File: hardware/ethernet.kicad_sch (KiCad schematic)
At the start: 92 parts, among them J5 USB_C_Receptacle, Q1 BSS138, Q2 BSS138, U11 TXS0202YZPR, U14 KSZ9031RNXCA, U4 GateMate-CCGM1A1, X1 ECS-2520MV-250-xx

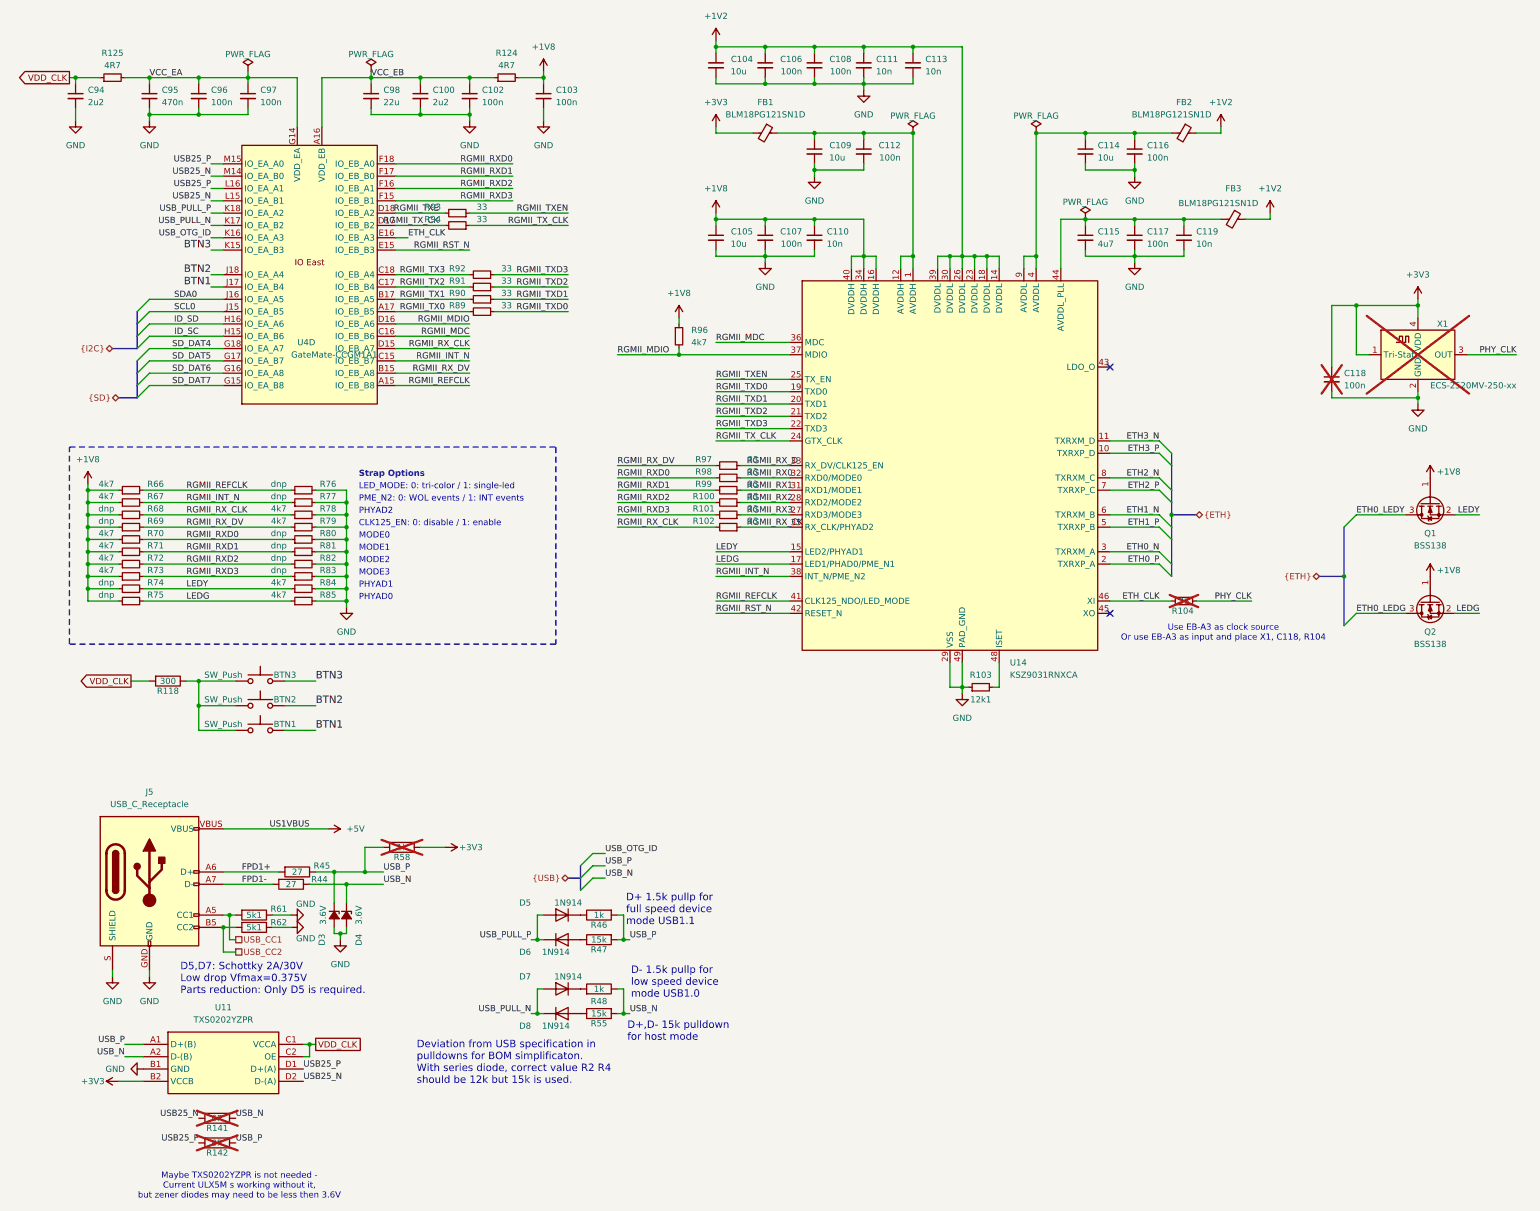
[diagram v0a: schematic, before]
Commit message: Updating sch - moving power select resistors to bottom
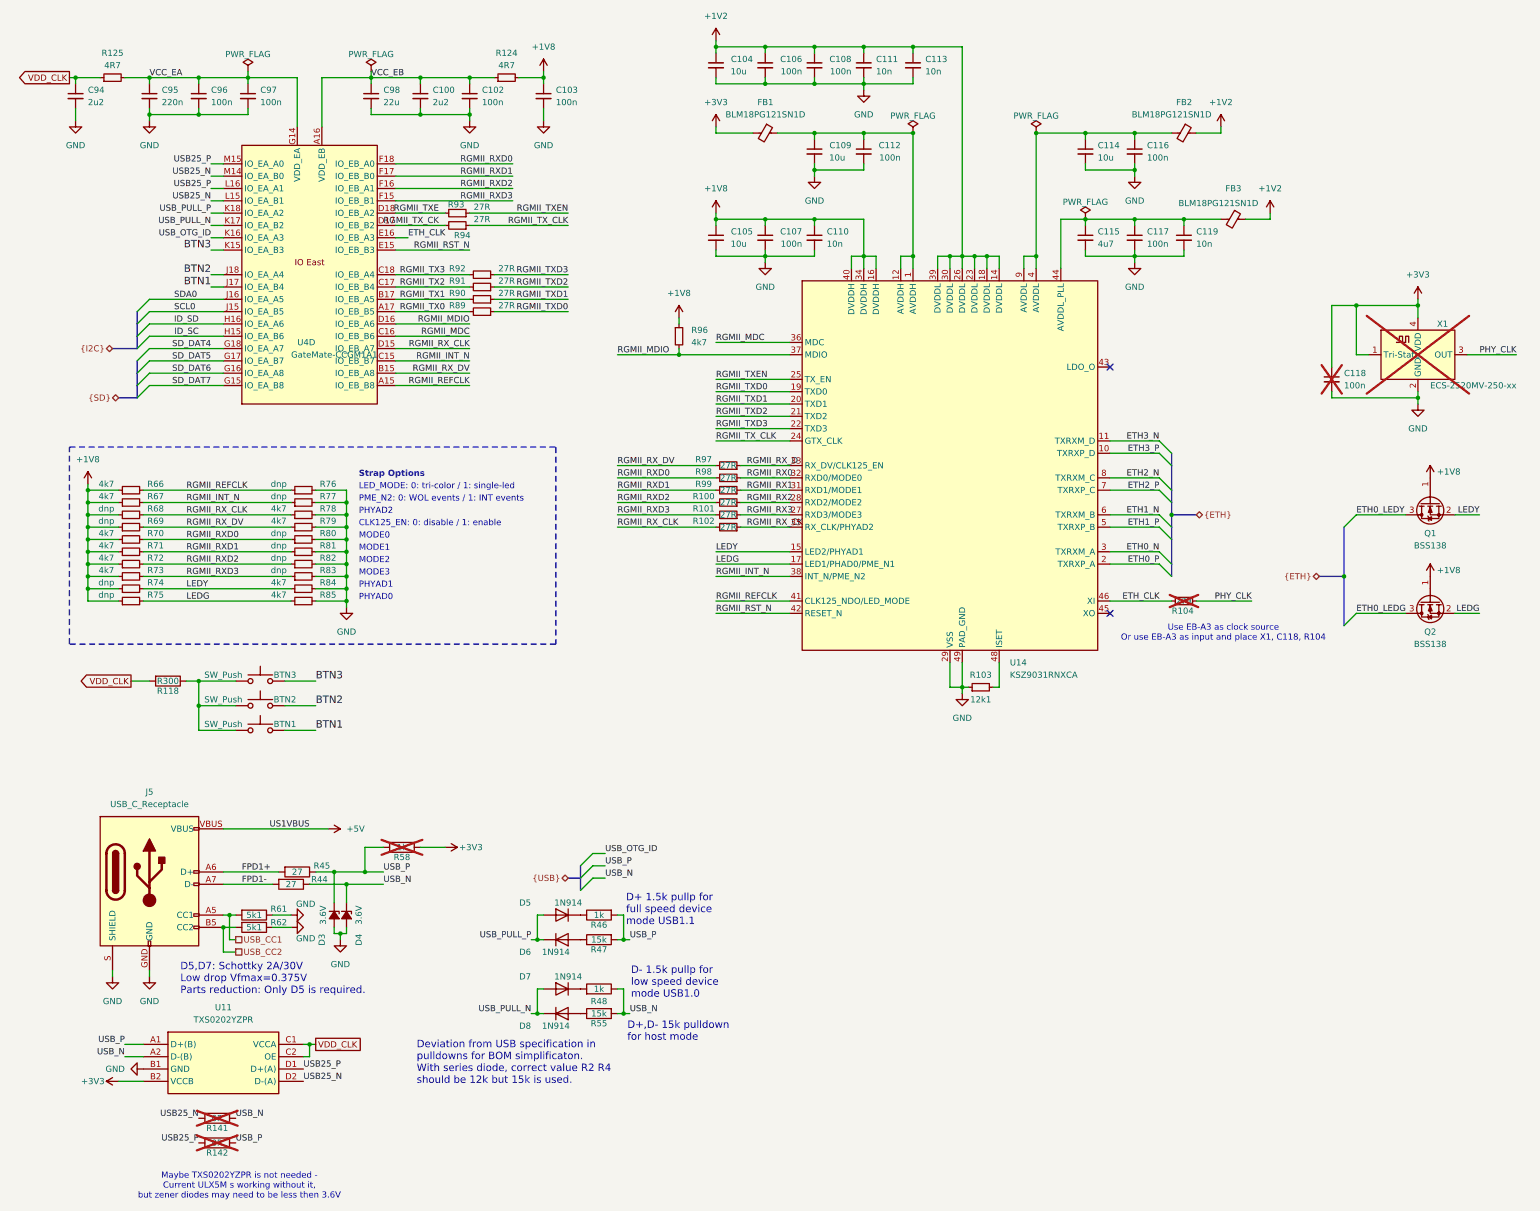
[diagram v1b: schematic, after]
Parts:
- C95: value 470n -> 220n
- R100, R101, R102, R104, R89, R90, R91, R92, R93, R94, R97, R98, R99: value 33 -> 27R
- R118: value 300 -> R300
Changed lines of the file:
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@@
 		(fields_autoplaced yes)
 		(property "Reference" "C95"
-			(at 43.18 29.2163 0)
+			(at 43.18 29.2162 0)
 			(effects
 				(font
@@
 			)
 		)
-		(property "Value" "470n"
-			(at 43.18 31.7563 0)
+		(property "Value" "220n"
+			(at 43.18 31.7562 0)
 			(effects
 				(font
@@
 		(dnp no)
 		(property "Reference" "R93"
-			(at 99.06 53.34 90)
+			(at 103.886 52.832 90)
 			(effects
 				(font
@@
 			)
 		)
-		(property "Value" "33"
+		(property "Value" "27R"
 			(at 109.22 53.34 90)
 			(effects
@@
 			)
 		)
-		(property "Value" "33"
-			(at 165.1 110.49 90)
+		(property "Value" "27R"
+			(at 160.02 111.76 90)
 			(effects
 				(font
@@
 			)
 		)
-		(property "Value" "33"
-			(at 165.1 107.95 90)
+		(property "Value" "27R"
+			(at 160.02 109.22 90)
 			(effects
 				(font
@@
 			)
 		)
-		(property "Value" "300"
+		(property "Value" "R300"
 			(at 44.45 151.13 90)
 			(effects
@@
 			)
 		)
-		(property "Value" "33"
+		(property "Value" "27R"
 			(at 114.3 73.66 90)
 			(effects
@@
 			)
 		)
-		(property "Value" "33"
-			(at 165.1 115.57 90)
+		(property "Value" "27R"
+			(at 160.02 116.84 90)
 			(effects
 				(font
@@
 			)
 		)
-		(property "Value" "33"
+		(property "Value" "27R"
 			(at 114.3 71.12 90)
 			(effects
@@
 			)
 		)
-		(property "Value" "33"
-			(at 165.1 113.03 90)
+		(property "Value" "27R"
+			(at 160.02 114.3 90)
 			(effects
 				(font
@@
 			)
 		)
-		(property "Value" "33"
+		(property "Value" "27R"
 			(at 114.3 68.58 90)
 			(effects
@@
 			)
 		)
-		(property "Value" "33"
+		(property "Value" "27R"
 			(at 114.3 66.04 90)
 			(effects
@@
 			)
 		)
-		(property "Value" "33"
+		(property "Value" "27R"
 			(at 254 134.62 90)
 			(effects
@@
 			)
 		)
-		(property "Value" "33"
-			(at 165.1 118.11 90)
+		(property "Value" "27R"
+			(at 160.02 119.38 90)
 			(effects
 				(font
@@
 			)
 		)
-		(property "Value" "33"
-			(at 165.1 105.41 90)
+		(property "Value" "27R"
+			(at 160.02 106.68 90)
 			(effects
 				(font
@@
 		(dnp no)
 		(property "Reference" "R94"
-			(at 99.06 55.88 90)
+			(at 105.156 59.182 90)
 			(effects
 				(font
@@
 			)
 		)
-		(property "Value" "33"
+		(property "Value" "27R"
 			(at 109.22 55.88 90)
 			(effects

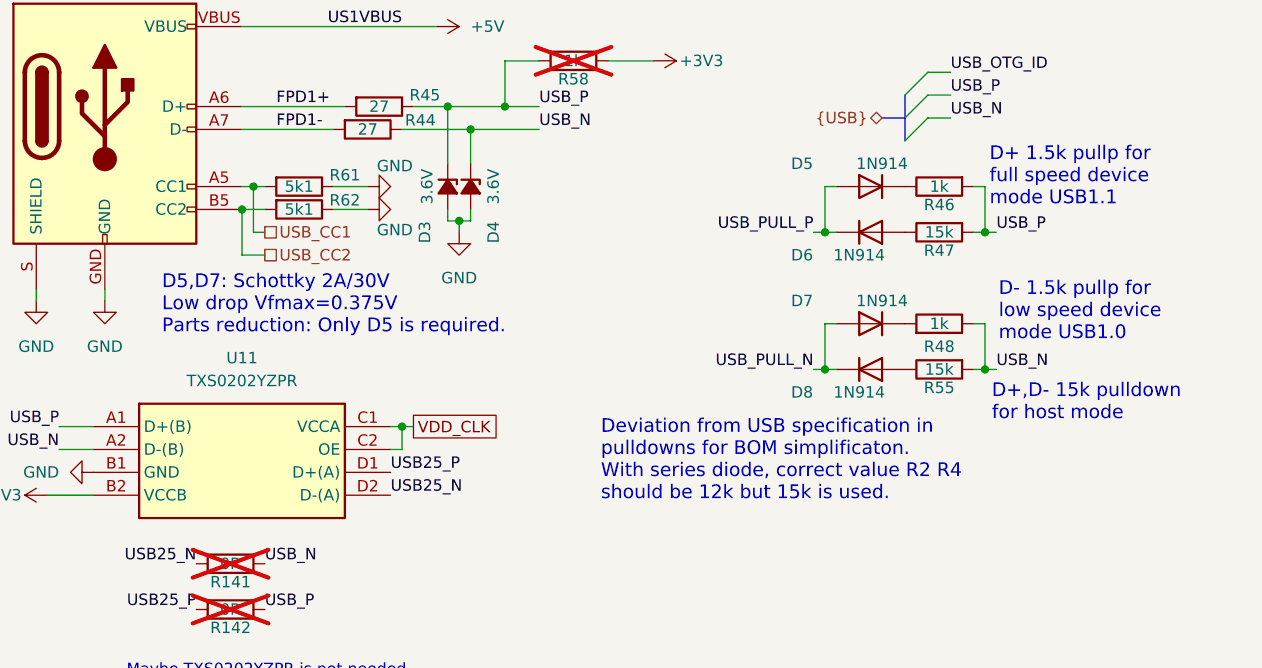
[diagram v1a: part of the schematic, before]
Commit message: USB PULL resistors can now be 12K
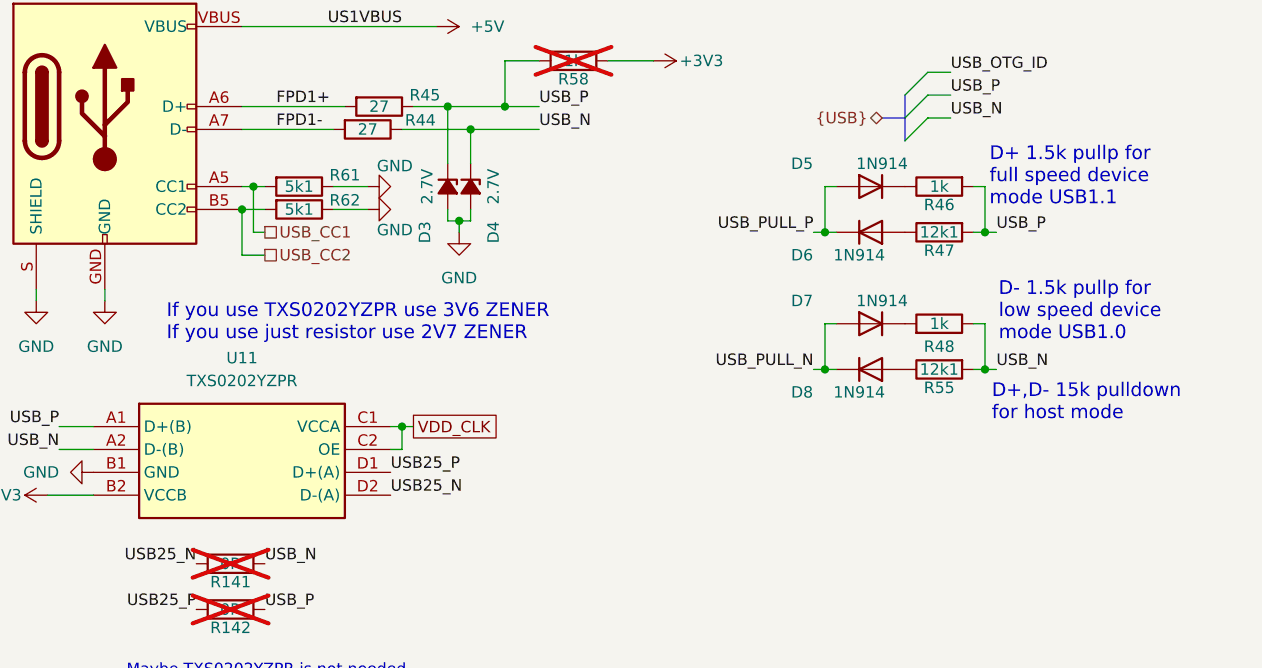
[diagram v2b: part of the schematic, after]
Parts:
- D3, D4: value 3.6V -> 2.7V
- R47, R55: value 15k -> 12k1
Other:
- note added: "If you use TXS0202YZPR use 3V6 ZENER If you use just resistor use 2V7 ZENER"
- note removed: "D5,D7: Schottky 2A/30V Low drop Vfmax=0.375V Parts reduction: Only D5 is required."
- note removed: "Deviation from USB specification in pulldowns for BOM simplificaton. With series diode, correct value R2 R4 should be 12k but 15k is used."
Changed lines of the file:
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@@
 		)
 	)
-	(text "Deviation from USB specification in\npulldowns for BOM simplificaton.\nWith series diode, correct value R2 R4 \nshould be 12k but 15k is used."
-		(exclude_from_sim no)
-		(at 95.758 234.442 0)
-		(effects
-			(font
-				(size 1.524 1.524)
-			)
-			(justify left bottom)
-		)
-	)
 	(text "MODE0"
 		(exclude_from_sim no)
@@
 		)
 	)
+	(text "If you use TXS0202YZPR use 3V6 ZENER\nIf you use just resistor use 2V7 ZENER"
+		(exclude_from_sim no)
+		(at 47.498 216.662 0)
+		(effects
+			(font
+				(size 1.524 1.524)
+			)
+			(justify left bottom)
+		)
+	)
 	(text "MODE2"
 		(exclude_from_sim no)
@@
 		)
 	)
-	(text "D5,D7: Schottky 2A/30V \nLow drop Vfmax=0.375V\nParts reduction: Only D5 is required."
-		(exclude_from_sim no)
-		(at 46.99 215.9 0)
-		(effects
-			(font
-				(size 1.524 1.524)
-			)
-			(justify left bottom)
-		)
-	)
 	(text "D- 1.5k pullp for \nlow speed device\nmode USB1.0"
 		(exclude_from_sim no)
@@
 			)
 		)
-		(property "Value" "3.6V"
+		(property "Value" "2.7V"
 			(at 76.454 199.39 0)
 			(effects
@@
 			)
 		)
-		(property "Value" "15k"
+		(property "Value" "12k1"
 			(at 133.35 219.71 90)
 			(effects
@@
 			)
 		)
-		(property "Value" "3.6V"
+		(property "Value" "2.7V"
 			(at 83.82 199.39 0)
 			(effects
@@
 			)
 		)
-		(property "Value" "15k"
+		(property "Value" "12k1"
 			(at 133.35 204.47 90)
 			(effects

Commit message: Fix #19
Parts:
- added R144, R145, R146: 1K, Resistor_SMD:R_0402_1005Metric, symbol Device:R
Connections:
- net BTN1: now also R144.2
- net BTN2: now also R145.2
- net BTN3: now also R146.2
- net GND: now also R118.2
- net VDD_CLK: now also R144.1, R145.1, R146.1; no longer R118.2
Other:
- moved on the sheet: BTN1, BTN2, BTN3, R118

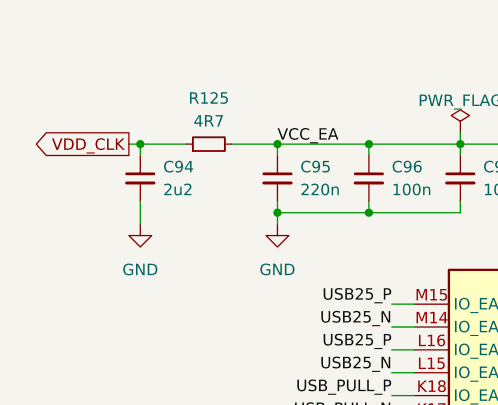
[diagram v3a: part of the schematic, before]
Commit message: Moving VCC_EA to 3.3V - USB and GPIO #27
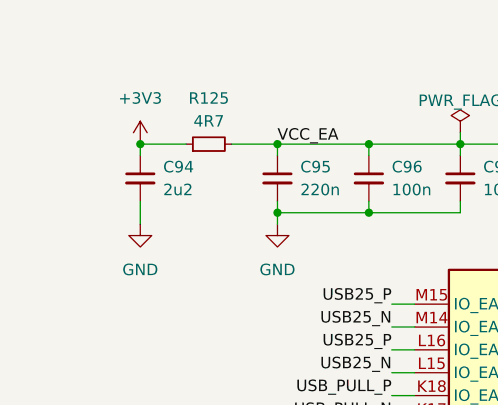
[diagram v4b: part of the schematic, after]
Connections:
- net +3V3: now also C94.1, R125.1
- net VDD_CLK: no longer C94.1, R125.1
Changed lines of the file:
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@@
 	(wire
 		(pts
-			(xy 25.4 26.67) (xy 24.13 26.67)
-		)
-		(stroke
-			(width 0)
-			(type default)
-		)
-	)
-	(wire
-		(pts
 			(xy 120.65 219.71) (xy 121.92 219.71)
 		)
@@
 	)
 	(global_label "VDD_CLK"
-		(shape output)
-		(at 24.13 26.67 180)
-		(fields_autoplaced yes)
-		(effects
-			(font
-				(size 1.27 1.27)
-			)
-			(justify right)
-		)
-		(property "Intersheetrefs" "${INTERSHEET_REFS}"
-			(at 12.9805 26.67 0)
-			(effects
-				(font
-					(size 1.27 1.27)
-				)
-				(justify right)
-				(hide yes)
-			)
-		)
-	)
-	(global_label "VDD_CLK"
 		(shape passive)
 		(at 74.93 226.06 0)
@@
 					(unit 1)
 				)
+			)
+		)
+	)
+	(symbol
+		(lib_name "+3V3_1")
+		(lib_id "power:+3V3")
+		(at 25.4 26.67 0)
+		(unit 1)
+		(exclude_from_sim no)
+		(in_bom yes)
+		(on_board yes)
+		(dnp no)
+		(fields_autoplaced yes)
+		(property "Reference" "#PWR082"
+			(at 25.4 30.48 0)
+			(effects
+				(font
+					(size 1.27 1.27)
+				)
+				(hide yes)
+			)
+		)
+		(property "Value" "+3V3"
+			(at 25.4 21.59 0)
+			(effects
+				(font
+					(size 1.27 1.27)
+				)
+			)
+		)
+		(property "Footprint" ""
+			(at 25.4 26.67 0)
+			(effects
+				(font
+					(size 1.27 1.27)
+				)
+				(hide yes)
+			)
+		)
+		(property "Datasheet" ""
+			(at 25.4 26.67 0)
+			(effects
+				(font
+					(size 1.27 1.27)
+				)
+				(hide yes)
+			)
+		)
+		(property "Description" "Power symbol creates a global label with name \"+3V3\""
+			(at 25.4 26.67 0)
+			(effects
+				(font
+					(size 1.27 1.27)
+				)
+				(hide yes)
+			)
+		)
+		(pin "1"
+		)
+		(instances
+			(project "ulx5m-gs"
+				(path "/9e5cbfd6-8186-4817-919e-acd256336bc8/5c4580e2-a442-496c-941e-38ded55dcc84"
+					(reference "#PWR082")
+					(unit 1)
+				)

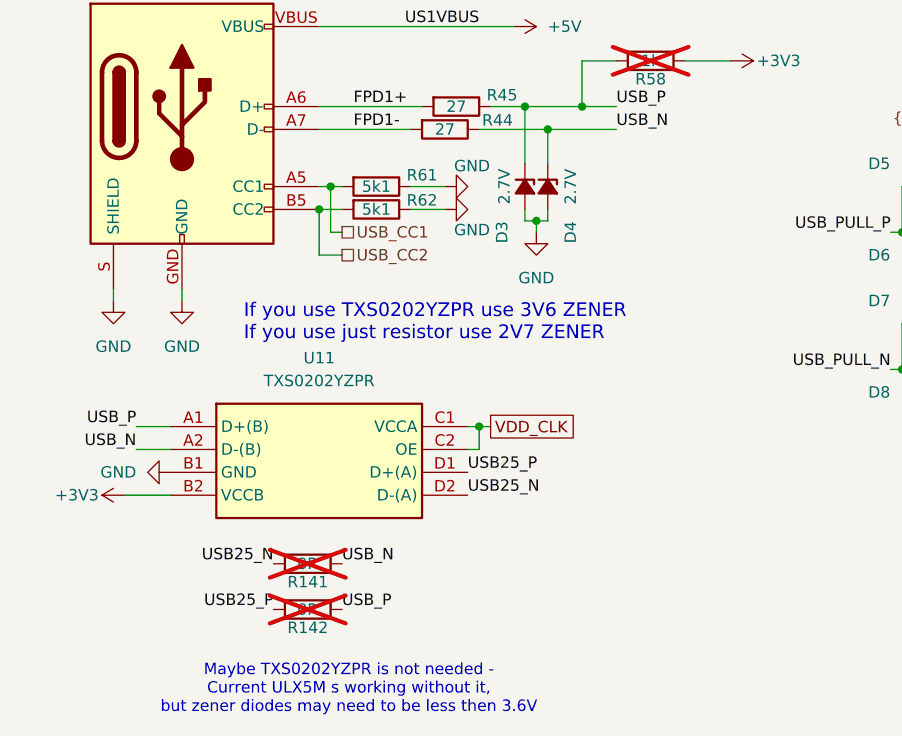
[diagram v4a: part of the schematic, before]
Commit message: Removing USB voltage tranalstion as now bank is on 3.3V #27
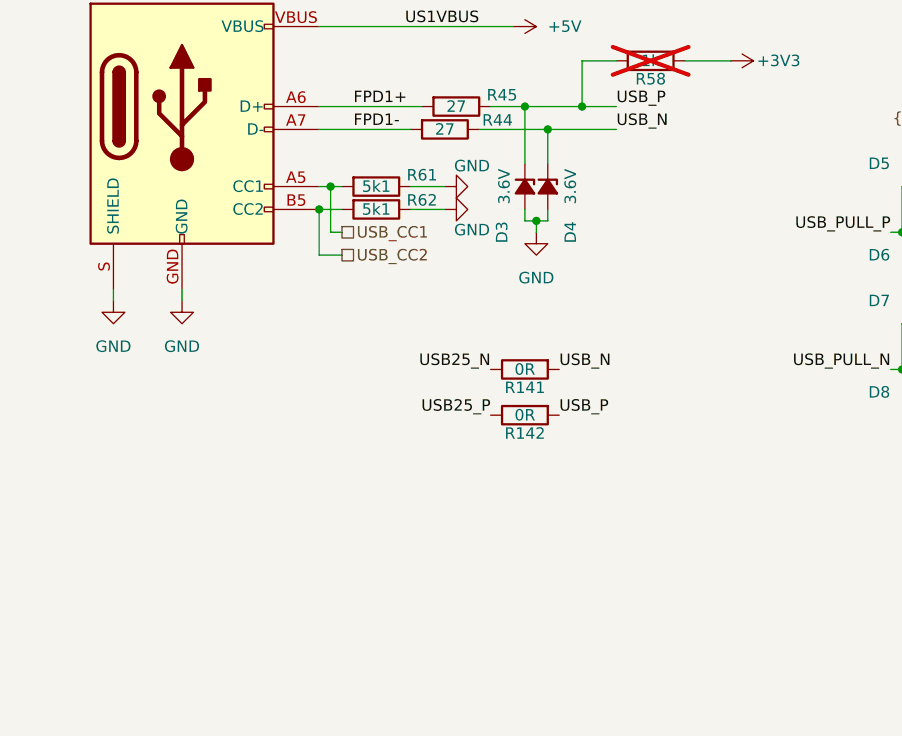
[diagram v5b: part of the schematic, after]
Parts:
- removed U11: TXS0202YZPR, TXS0202YZPR:BGA8C50P2X4_89X189X50, symbol TXS0202YZPR:TXS0202YZPR
- D3, D4: value 2.7V -> 3.6V
- R141, R142: now fitted
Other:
- note removed: "If you use TXS0202YZPR use 3V6 ZENER If you use just resistor use 2V7 ZENER"
- note removed: "Maybe TXS0202YZPR is not needed - Current ULX5M s working without it, but zener diodes may need to be less then 3.6V"

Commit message: CleanUP
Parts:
- removed R124, R125: 4R7, Resistor_SMD:R_0402_1005Metric, symbol Device:R_Small
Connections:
- net VCC_EA is gone; now on net +3V3: C95.1, C96.1, C97.1, U4.G14 (VDD_EA), U4.H17 (VDD_EA), U4.J14 (VDD_EA), U4.L14 (VDD_EA), U4.L17 (VDD_EA)
- net VCC_EB is gone; now on net +1V8: C100.1, C102.1, C98.1, U4.A16 (VDD_EB), U4.B18 (VDD_EB), U4.E14 (VDD_EB), U4.E17 (VDD_EB), U4.F13 (VDD_EB)
- net SD_DAT4 renamed PWR_BTN
- net SD_DAT5: no longer names the net of U4.G17 (IO_EA_B7)
- net SD_DAT6: no longer names the net of U4.G16 (IO_EA_A8)
- net SD_DAT7: no longer names the net of U4.G15 (IO_EA_B8)
